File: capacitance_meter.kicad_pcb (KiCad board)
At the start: 2 copper layers, 35 x 14 mm, 15 parts, among them J1 Conn_02x04_Counter_Clockwise, J2 Conn_02x04_Counter_Clockwise, J3 Conn_01x06_Male, U1 FDC1004, U2 TCN75AVUA713, U3 FDC1004

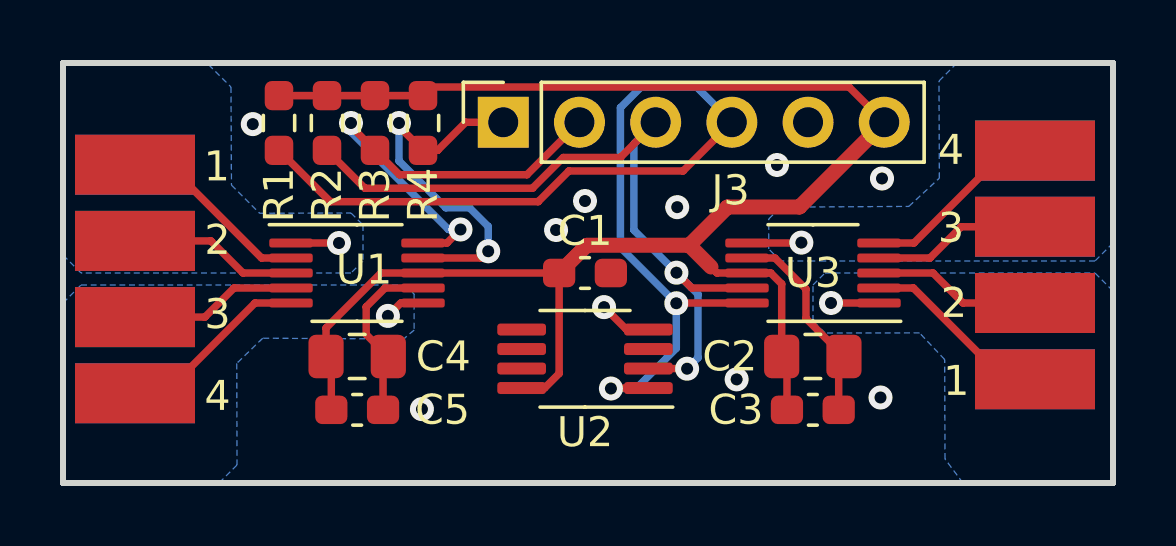
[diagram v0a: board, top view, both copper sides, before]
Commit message: added termal cutouts to pcb
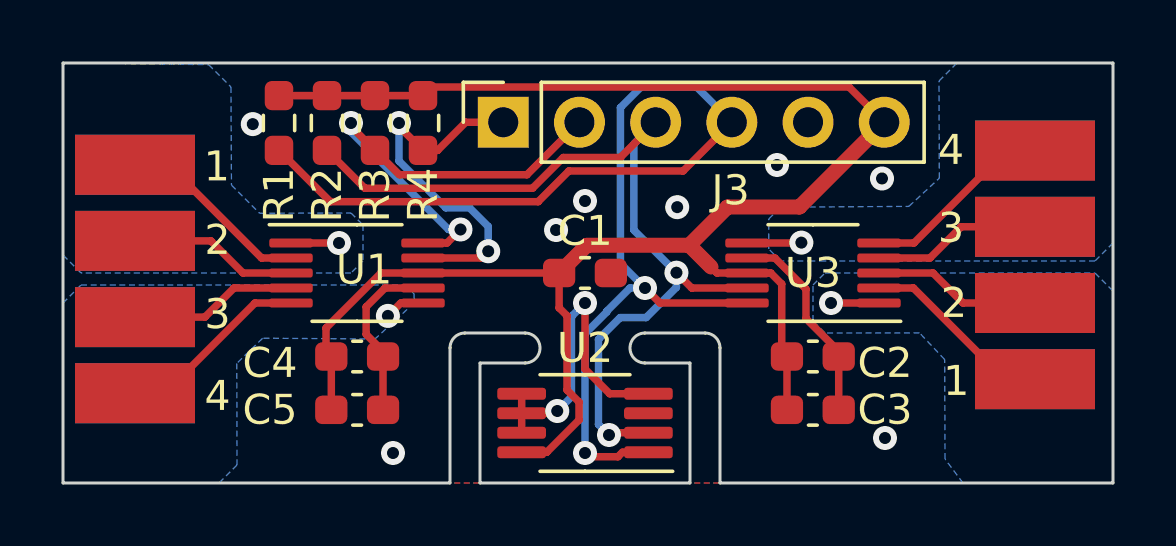
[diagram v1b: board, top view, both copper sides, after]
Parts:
- C2, C4: footprint Capacitor_SMD:C_0805_2012Metric_Pad1.18x1.45mm_HandSolder -> Capacitor_SMD:C_0603_1608Metric_Pad1.08x0.95mm_HandSolder
- moved U2 2.14 mm to (154.0, 125.0)
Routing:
- net GND: track 14.8 -> 24.1 mm
- net /SDA1: track 36.5 -> 40.2 mm
- net /SCL1: track 25.8 -> 29.3 mm
- net VDD: track 57.7 -> 60.4 mm
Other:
- outline, holes or cut-outs redrawn

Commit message: added datasheet images
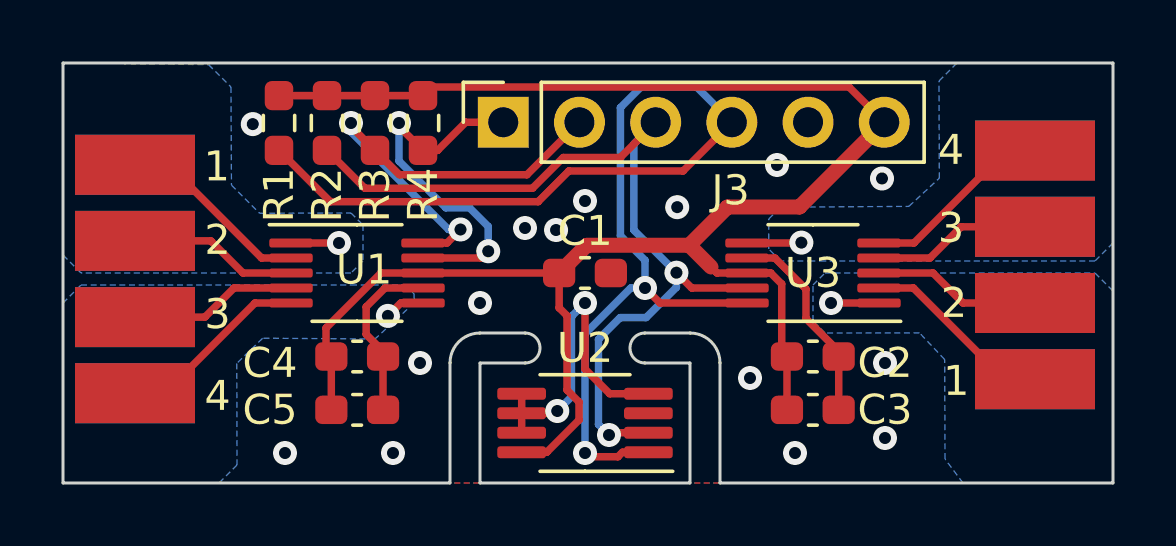
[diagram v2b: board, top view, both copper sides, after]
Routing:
- net GND: vias 10 -> 17
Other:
- outline, holes or cut-outs redrawn
